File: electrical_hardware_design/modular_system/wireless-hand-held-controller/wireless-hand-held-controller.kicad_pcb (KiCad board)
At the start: 4 copper layers, 79.4 x 71.1 mm, 58 parts, among them J1 328P_Prog_Pins, J2 328P_Bootloader_Pins, J3 Input Power, J4 2560_Prog_Pins, J5 2560_Bootloader_Pins, J6 Speaker Conn, J7 INT_PWR_CON, J8 External_Interrupts, U1 L7805CV, U2 AMS1117-3.3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

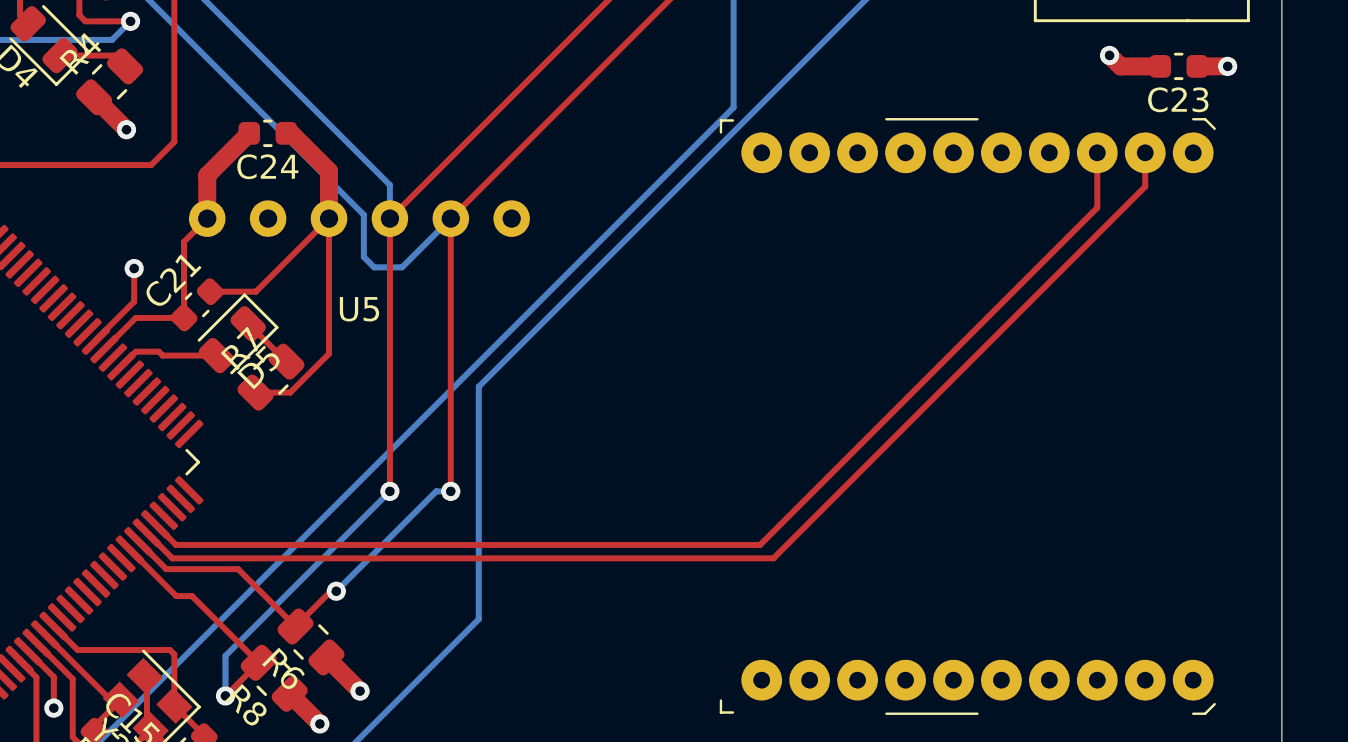
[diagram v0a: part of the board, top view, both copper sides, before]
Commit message: add logic level shifters for xbee
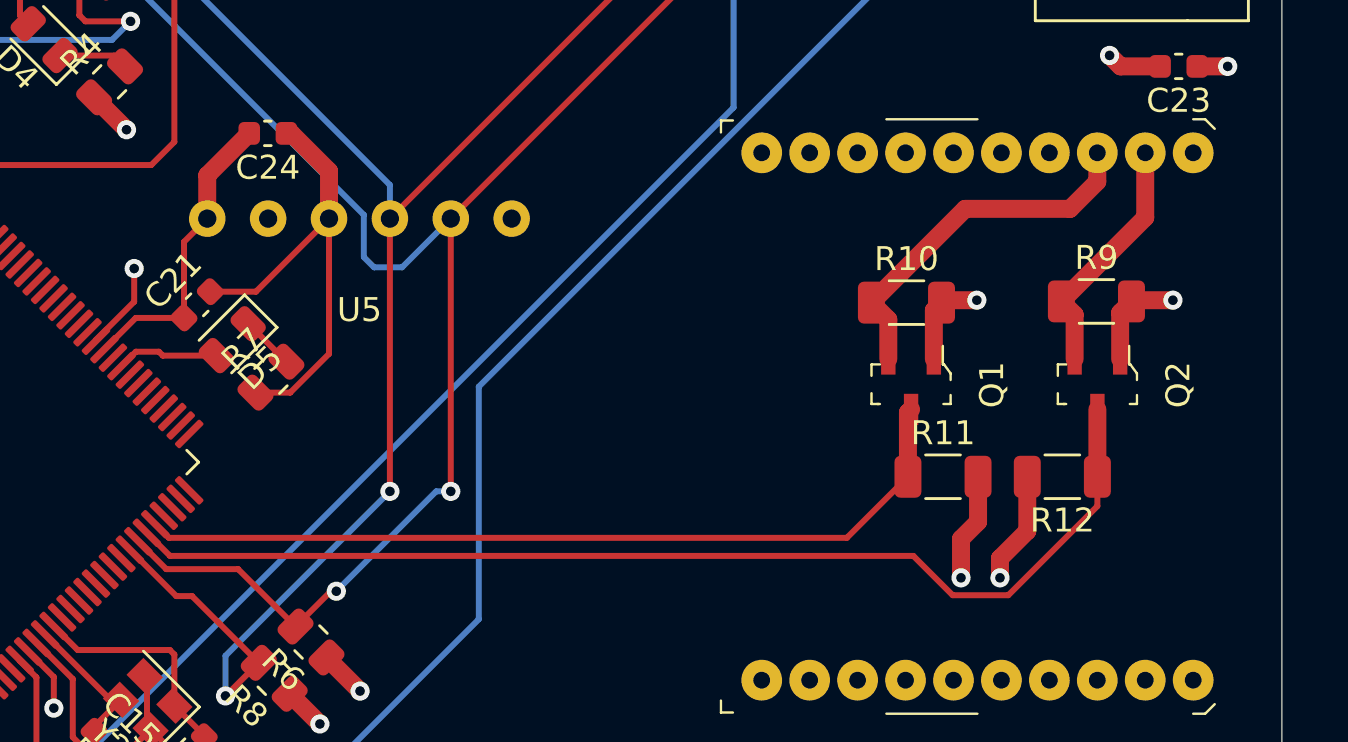
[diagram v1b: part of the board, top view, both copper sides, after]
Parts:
- added Q1: BSS138, digikey-footprints:SOT-23-3, F.Cu at (173.1, 136.4)
- added Q2: BSS138, digikey-footprints:SOT-23-3, F.Cu at (180.9, 136.4)
- added R10: 10k, Resistor_SMD:R_1206_3216Metric, F.Cu at (172.9, 133.0)
- added R11: 10k, Resistor_SMD:R_1206_3216Metric, F.Cu at (174.5, 140.3)
- added R12: 10k, Resistor_SMD:R_1206_3216Metric, F.Cu at (179.4, 140.3)
- added R9: 10k, Resistor_SMD:R_1206_3216Metric, F.Cu at (180.9, 133.0)
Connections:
- MOD1 pad 2: XBEE_TX -> XBEE_TX_3.3V
- MOD1 pad 3: XBEE_RX -> XBEE_RX_3.3V
- U4 pad 45: XBEE_TX -> XBEE_TX_5V
- U4 pad 46: XBEE_RX -> XBEE_RX_5V
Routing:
- net XBEE_TX: track 49.9 -> 0.00 mm
- net +5V: track 126.7 -> 174.6 mm, vias 25 -> 27
- net XBEE_RX: track 47.8 -> 0.00 mm
- net XBEE_TX_5V: track 0.00 -> 46.3 mm
- net XBEE_RX_5V: track 0.00 -> 35.6 mm
- net +3V3: track 65.4 -> 88.5 mm, vias 17 -> 19
- net XBEE_RX_3.3V: track 0.00 -> 15.4 mm
- net XBEE_TX_3.3V: track 0.00 -> 10.3 mm
